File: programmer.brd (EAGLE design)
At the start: 45.7 x 20.3 mm, 23 parts, among them IC1 74241, U1 ATMEGA8U2, X2 SPARKFUN_USB-MICROB, Y1 16MHz

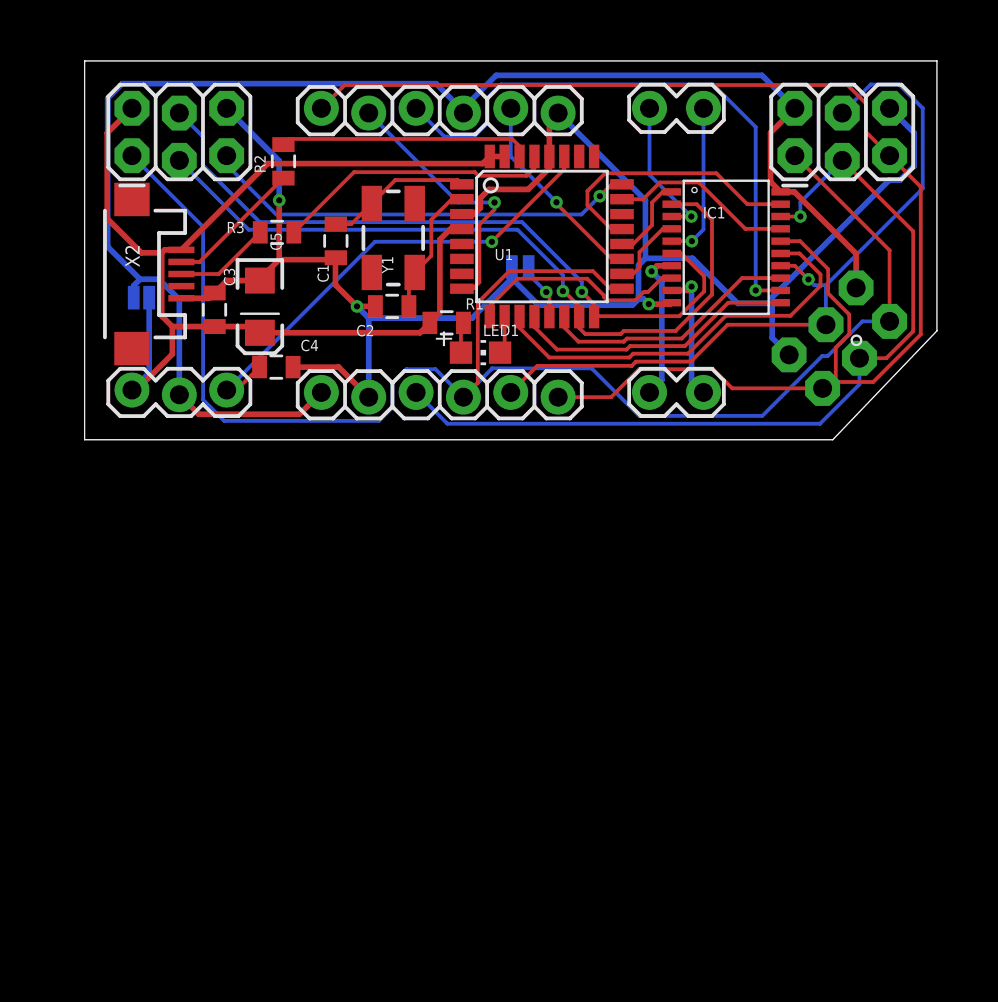
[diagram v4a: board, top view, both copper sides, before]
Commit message: 8 mil traces, 14 vias, beveled corners
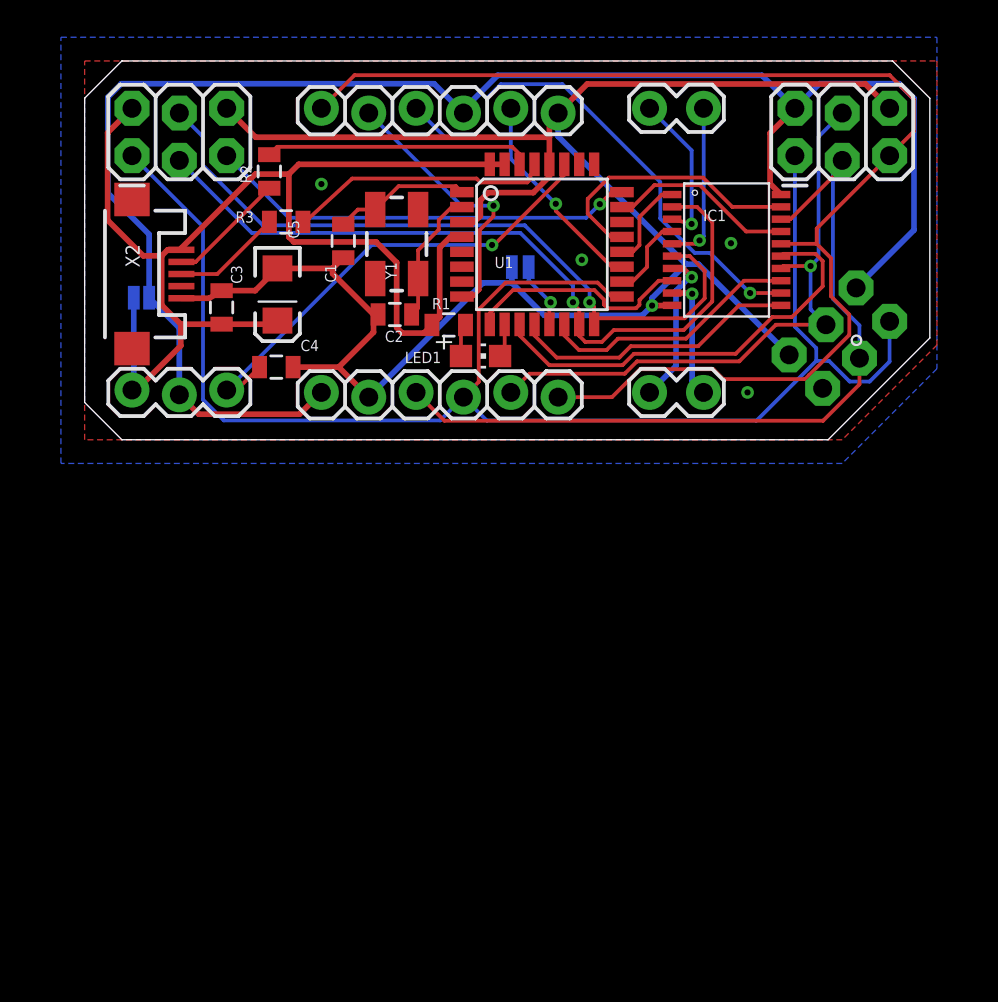
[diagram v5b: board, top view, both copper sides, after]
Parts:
- moved C5 1.15 mm to (10.3, 7.79)
- moved R2 0.93 mm to (9.91, 14.4)
- moved R3 0.74 mm to (10.8, 11.7)
- moved C2 0.46 mm to (16.6, 6.72)
- moved U1 0.42 mm to (24.5, 10.5)
- moved C3 0.40 mm to (7.35, 7.10)
- moved C1 0.40 mm to (13.9, 10.7)
- moved Y1 0.37 mm to (16.7, 10.5)
- moved LED1 0.18 mm to (21.2, 4.49)
- moved R1 0.16 mm to (19.5, 6.16)
- moved IC1 0.14 mm to (34.5, 10.5)
- turned SJ1 to 180 degrees
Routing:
- net GND: track 97.7 -> 110.3 mm, vias 3 -> 5
- net VCC: track 79.7 -> 89.7 mm
- net MOSI/TDI-B: track 40.5 -> 32.9 mm
- net RST/TMS/DTR-B: track 75.4 -> 69.0 mm
- net 5V: track 64.9 -> 71.0 mm
- net TXO-B: track 31.8 -> 27.9 mm
- net SCK/TCK-B: track 46.0 -> 43.4 mm, vias 1 -> 0
- net MISO/TDO: track 83.5 -> 82.5 mm
- net D-RAW: track 7.34 -> 6.35 mm
- net XCK: track 22.2 -> 23.1 mm
- net D+: track 15.1 -> 14.3 mm
- net MOSI/TDI: track 37.9 -> 38.7 mm
- net D-: track 13.5 -> 14.3 mm
- net D+RAW: track 5.16 -> 5.88 mm
- net SCK/TCK: track 41.0 -> 41.7 mm
- added copper zone on layer 1, net GND
- added copper zone on layer 16, net GND
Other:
- board size 45.7 x 20.3 mm -> 45.3 x 20.3 mm
- board text added: "v1.0c"
- board text removed: "v1.0"

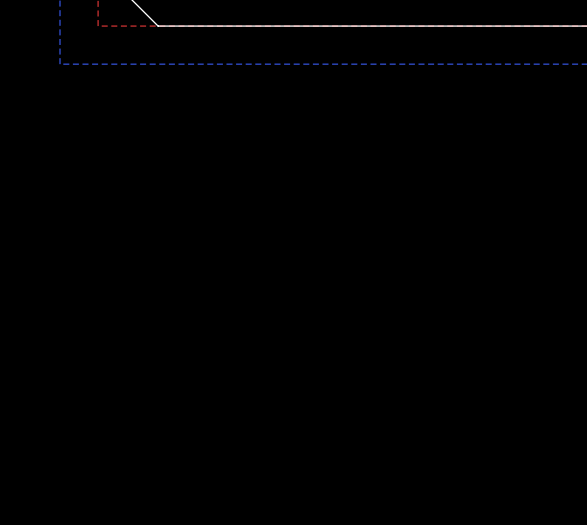
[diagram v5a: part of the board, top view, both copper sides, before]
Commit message: Various changes.
- Change VCC labels to VIO (https://github.com/sowbug/avr-programmer/issues/15).
- Change LED resistor from 1K to 330 (https://github.com/sowbug/avr-programmer/issues/16).
- Added second status LED (https://github.com/sowbug/avr-programmer/issues/9).
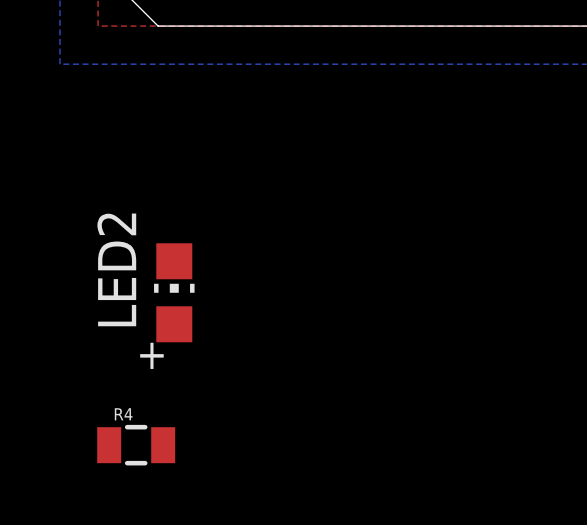
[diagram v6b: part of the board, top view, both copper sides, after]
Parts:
- added LED2: ACTIVITY, programmer:CHIP-LED0805
- added R4: 330, programmer:SPARKFUN_0805
- R1: value 1K -> 330
- SJ1: value VCC-5V -> VIO-5V
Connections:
- net ACTIVITY renamed ACT0
- new net ACT1: LED2.C, U1.6
- new net VCC-LED1: LED2.A, R4.1
- net 5V: now also R4.2
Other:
- board text added: "VIO"
- board text removed: "VCC"
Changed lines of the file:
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@@
 <text x="12.065" y="7.62" size="1.016" layer="22" font="vector" rot="MR0" align="bottom-right">RST 5</text>
 <text x="12.065" y="7.62" size="1.016" layer="22" font="vector" rot="MR0">6 GND</text>
-<text x="5.08" y="4.445" size="0.8128" layer="22" font="vector" rot="MR135" align="center">VCC</text>
+<text x="5.08" y="4.445" size="0.8128" layer="22" font="vector" rot="MR135" align="center">VIO</text>
 <text x="7.62" y="4.445" size="0.8128" layer="22" font="vector" rot="MR135" align="center">3V3</text>
-<text x="12.7" y="4.445" size="0.8128" layer="22" font="vector" rot="MR135" align="center">VCC</text>
+<text x="12.7" y="4.445" size="0.8128" layer="22" font="vector" rot="MR135" align="center">VIO</text>
 <text x="15.24" y="4.445" size="0.8128" layer="22" font="vector" rot="MR135" align="center">GND</text>
 <text x="17.78" y="4.445" size="0.8128" layer="22" font="vector" rot="MR135" align="center">TCK</text>
@@
 <text x="25.4" y="15.24" size="0.8128" layer="22" font="vector" rot="MR135" align="center">GND</text>
 <text x="22.86" y="15.24" size="0.8128" layer="22" font="vector" rot="MR135" align="center">CTS</text>
-<text x="20.32" y="15.24" size="0.8128" layer="22" font="vector" rot="MR135" align="center">VCC</text>
+<text x="20.32" y="15.24" size="0.8128" layer="22" font="vector" rot="MR135" align="center">VIO</text>
 <text x="17.78" y="15.24" size="0.8128" layer="22" font="vector" rot="MR135" align="center">TXO</text>
 <text x="15.24" y="15.24" size="0.8128" layer="22" font="vector" rot="MR135" align="center">RXI</text>
@@
 <attribute name="VALUE" x="10.9802" y="2.9442" size="0.6096" layer="27" font="vector" rot="R180"/>
 </element>
-<element name="R1" library="programmer" package="SPARKFUN_0805" value="1K" x="19.5304" y="6.1581" smashed="yes" rot="R180">
+<element name="R1" library="programmer" package="SPARKFUN_0805" value="330" x="19.5304" y="6.1581" smashed="yes" rot="R180">
 <attribute name="NAME" x="18.6342" y="7.0007" size="0.6" layer="25" font="vector"/>
 <attribute name="VALUE" x="18.6342" y="6.8737" size="0.6096" layer="27" font="vector"/>
@@
 <attribute name="NAME" x="2.19" y="10.49" size="0.762" layer="25" rot="R270"/>
 </element>
-<element name="SJ1" library="programmer" package="SPARKFUN_SJ_2S" value="VCC-5V" x="3.048" y="7.62" smashed="yes" rot="MR180">
+<element name="SJ1" library="programmer" package="SPARKFUN_SJ_2S" value="VIO-5V" x="3.048" y="7.62" smashed="yes" rot="MR180">
 <attribute name="NAME" x="0.5742" y="6.35" size="0.6096" layer="26" font="vector" rot="MR180"/>
 <attribute name="VALUE" x="0.5742" y="10.033" size="0.6096" layer="26" font="vector" rot="MR180"/>
@@
 <attribute name="VALUE" x="24.9989" y="10.9126" size="0.6096" layer="26" font="vector" rot="MR180"/>
 </element>
+<element name="R4" library="programmer" package="SPARKFUN_0805" value="330" x="1.27" y="-13.97"/>
+<element name="LED2" library="programmer" package="CHIP-LED0805" value="ACTIVITY" x="2.54" y="-8.89"/>
 </elements>
 <signals>
@@
 <wire x1="7.3467" y1="6.199" x2="10.1513" y2="6.199" width="0.3048" layer="1"/>
 <wire x1="10.1513" y1="6.199" x2="10.3442" y2="6.3919" width="0.3048" layer="1"/>
+<contactref element="R4" pad="2"/>
+<wire x1="2.54" y1="2.667" x2="2.17" y2="-13.97" width="0" layer="19" extent="1-16"/>
 </signal>
 <signal name="RST/TMS/DTR-B">
@@
 <wire x1="30.994" y1="11.1722" x2="31.5141" y2="11.1722" width="0.2032" layer="1"/>
 </signal>
-<signal name="ACTIVITY">
+<signal name="ACT0">
 <contactref element="LED1" pad="C"/>
 <contactref element="U1" pad="10"/>
@@
 <via x="32.5897" y="7.8304" extent="1-16" drill="0.3302" diameter="0.6858"/>
 </signal>
+<signal name="VCC-LED1">
+<contactref element="R4" pad="1"/>
+<contactref element="LED2" pad="A"/>
+<wire x1="2.54" y1="-9.94" x2="0.37" y2="-13.97" width="0" layer="19" extent="1-1"/>
+</signal>
+<signal name="ACT1">
+<contactref element="U1" pad="6"/>
+<contactref element="LED2" pad="C"/>
+<wire x1="2.54" y1="-7.84" x2="20.2383" y2="9.2826" width="0" layer="19" extent="1-1"/>
+</signal>
 </signals>

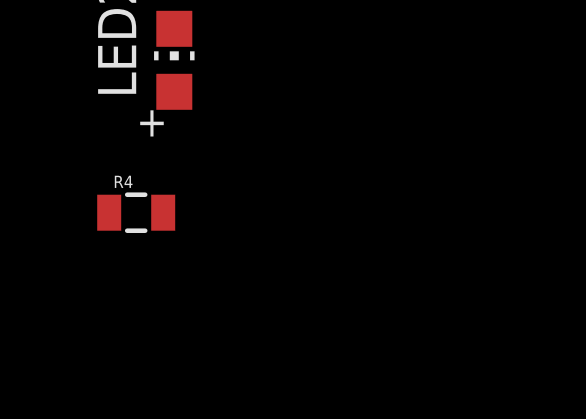
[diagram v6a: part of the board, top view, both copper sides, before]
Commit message: Add SJ3 for 3V3 -> VIO.
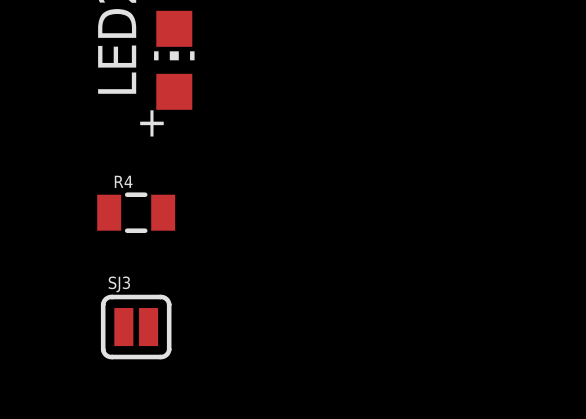
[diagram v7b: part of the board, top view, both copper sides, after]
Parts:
- added SJ3: VIO-3V3, programmer:SPARKFUN_SJ_2S
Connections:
- net 3.3V: now also SJ3.1
- net VCC: now also SJ3.2
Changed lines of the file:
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@@
 <element name="R4" library="programmer" package="SPARKFUN_0805" value="330" x="1.27" y="-13.97"/>
 <element name="LED2" library="programmer" package="CHIP-LED0805" value="ACTIVITY" x="2.54" y="-8.89"/>
+<element name="SJ3" library="programmer" package="SPARKFUN_SJ_2S" value="VIO-3V3" x="1.27" y="-17.78"/>
 </elements>
 <signals>
@@
 <wire x1="41.402" y1="8.128" x2="41.38395" y2="8.14605" width="0.3048" layer="16"/>
 <wire x1="41.402" y1="8.128" x2="41.3839" y2="8.1461" width="0.3048" layer="16"/>
+<contactref element="SJ3" pad="2"/>
+<wire x1="6.1216" y1="1.3714" x2="1.6819" y2="-17.78" width="0" layer="19" extent="1-1"/>
 </signal>
 <signal name="GND" class="1">
@@
 <wire x1="7.62" y1="2.667" x2="8.152" y2="2.667" width="0.2032" layer="1"/>
 <wire x1="8.152" y1="2.667" x2="9.3817" y2="3.8967" width="0.2032" layer="1"/>
+<contactref element="SJ3" pad="1"/>
+<wire x1="7.62" y1="2.667" x2="0.8581" y2="-17.78" width="0" layer="19" extent="1-16"/>
 </signal>
 <signal name="D-RAW">

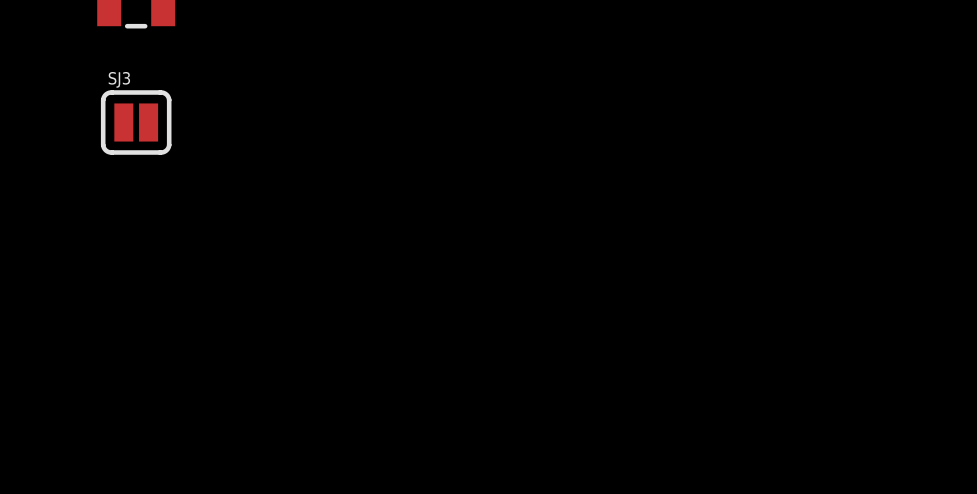
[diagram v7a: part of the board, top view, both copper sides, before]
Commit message: Added switch.
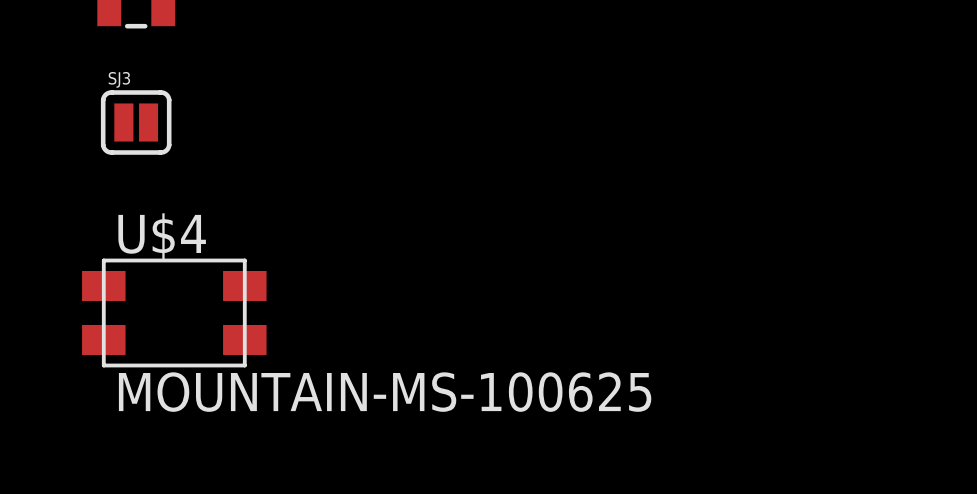
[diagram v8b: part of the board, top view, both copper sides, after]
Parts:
- added U$4: MOUNTAIN-MS-100625, programmer:MOUNTAIN-MS-100625
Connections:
- new net MODE: U$4.P$1, U$4.P$3, U1.7
- net GND: now also U$4.P$2, U$4.P$4
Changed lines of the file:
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@@
 <element name="LED2" library="programmer" package="CHIP-LED0805" value="ACTIVITY" x="2.54" y="-8.89"/>
 <element name="SJ3" library="programmer" package="SPARKFUN_SJ_2S" value="VIO-3V3" x="1.27" y="-17.78"/>
+<element name="U$4" library="programmer" package="MOUNTAIN-MS-100625" value="MOUNTAIN-MS-100625" x="2.54" y="-24.13"/>
 </elements>
 <signals>
@@
 <via x="26.67" y="9.652" extent="1-16" drill="0.3302" diameter="0.6858"/>
 <via x="12.7" y="13.716" extent="1-16" drill="0.3302" diameter="0.6858"/>
+<contactref element="U$4" pad="P$4"/>
+<contactref element="U$4" pad="P$2"/>
+<wire x1="32.9274" y1="9.4183" x2="34.671" y2="10.541" width="0" layer="19" extent="16-16"/>
+<wire x1="37.791846875" y1="4.553946875" x2="37.7918" y2="4.5539" width="0" layer="19" extent="16-16"/>
+<wire x1="35.56" y1="2.54" x2="37.7918" y2="4.5539" width="0" layer="19" extent="16-16"/>
+<wire x1="26.67" y1="9.652" x2="24.6612" y2="6.674" width="0" layer="19" extent="16-16"/>
+<wire x1="12.7" y1="13.716" x2="13.8734" y2="9.7645" width="0" layer="19" extent="1-1"/>
+<wire x1="4.89" y1="-25.03" x2="15.24" y2="2.286" width="0" layer="19" extent="1-16"/>
+<wire x1="0.19" y1="-25.03" x2="4.89" y2="-25.03" width="0" layer="19" extent="1-1"/>
 </signal>
 <signal name="D+RAW">
@@
 <wire x1="2.54" y1="-7.84" x2="20.2383" y2="9.2826" width="0" layer="19" extent="1-1"/>
 </signal>
+<signal name="MODE">
+<contactref element="U$4" pad="P$1"/>
+<contactref element="U$4" pad="P$3"/>
+<contactref element="U1" pad="7"/>
+<wire x1="4.89" y1="-23.23" x2="20.2383" y2="8.4826" width="0" layer="19" extent="1-1"/>
+<wire x1="0.19" y1="-23.23" x2="4.89" y2="-23.23" width="0" layer="19" extent="1-1"/>
+</signal>
 </signals>
